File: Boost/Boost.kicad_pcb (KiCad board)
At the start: 4 copper layers, 32 x 59 mm, 22 parts, among them J1 Conn_02x04_Odd_Even, J2 Conn_02x04_Odd_Even, SW1 ON-OFF-ON, U1 OPA1655

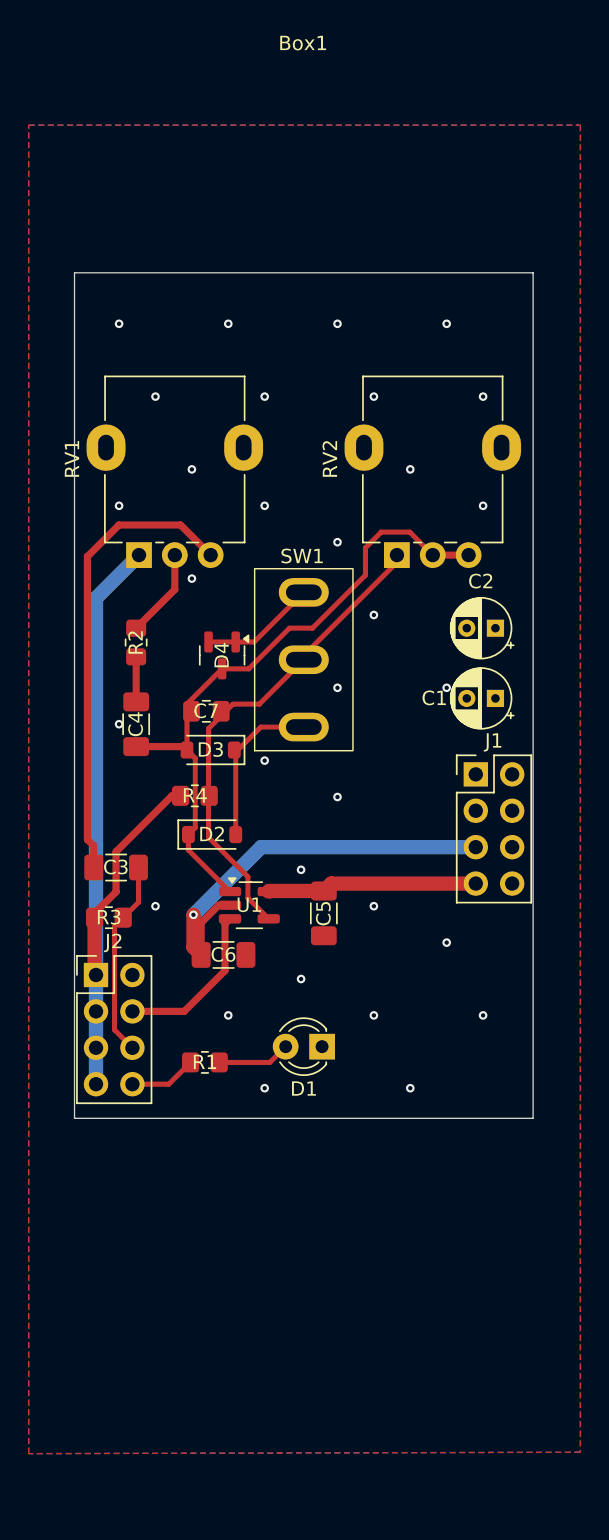
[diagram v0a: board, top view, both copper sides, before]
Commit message: Add tentative drill patterns for Tayda enclosure drilling
Fix up the layout so that the same drill pattern with three holes for
pots/switches works for both the Baxandall and Boost, and move some of
the other controls around to make for whole numbers in mm.

Do the drill patterns work? They match the PCB layout, but let's see
about the vertical sides...  Tayda drilling is running behind, so I
don't think I'll see the actual result for a couple of weeks.

Also fix some typos in the readme while updating it about the drill
patterns.

Signed-off-by: Linus Torvalds <torvalds@linux-foundation.org>
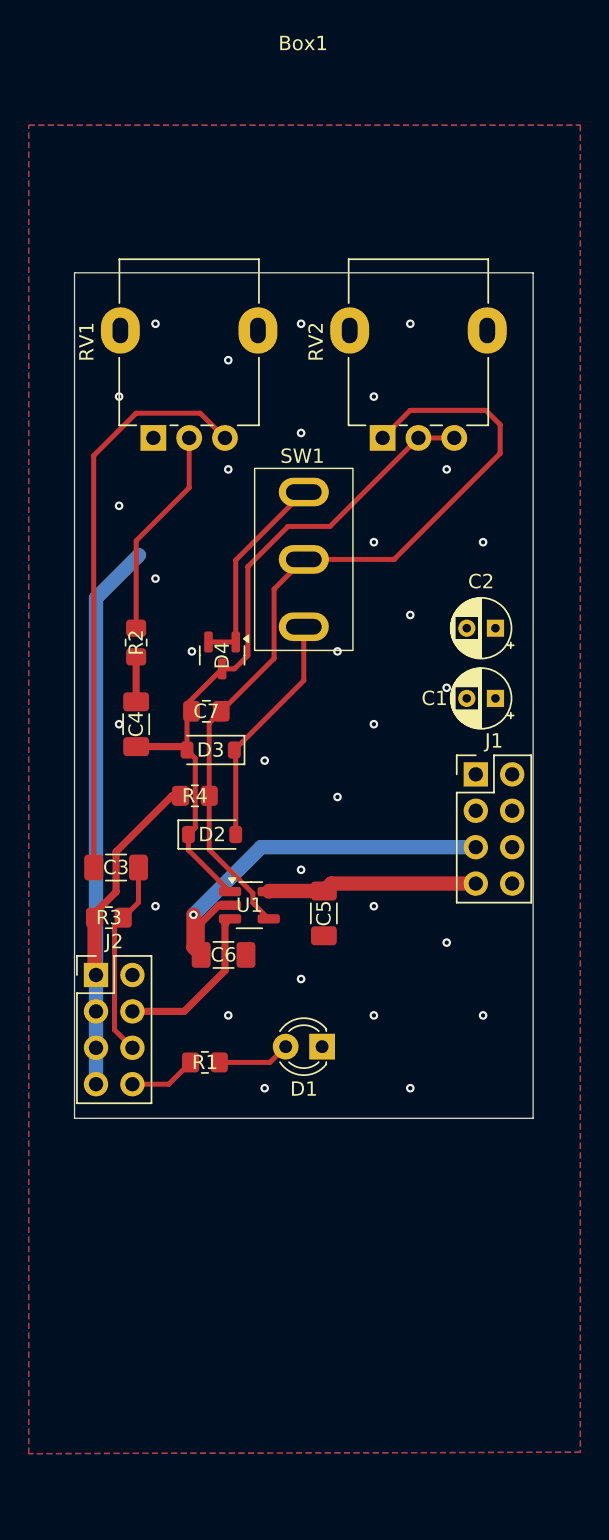
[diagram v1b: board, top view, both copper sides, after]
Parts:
- moved RV1 8.24 mm to (189.5, 75.5)
- moved RV2 8.24 mm to (205.5, 75.5)
- moved SW1 7.00 mm to (200.0, 84.0)
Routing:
- net Net-(SW1-B): track 33.3 -> 57.7 mm
- net Net-(R2-Pad2): track 6.22 -> 14.8 mm
- net Net-(C3-Pad1): track 32.3 -> 39.8 mm
- net Net-(D4-A): track 8.08 -> 14.3 mm
- net Net-(D2-A): track 11.1 -> 16.4 mm
- net Net-(D2-K): track 44.8 -> 48.3 mm
